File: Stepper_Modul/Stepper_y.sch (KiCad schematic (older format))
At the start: 14 parts, among them SW501 SW_DIP_x03, U501 TMC2226

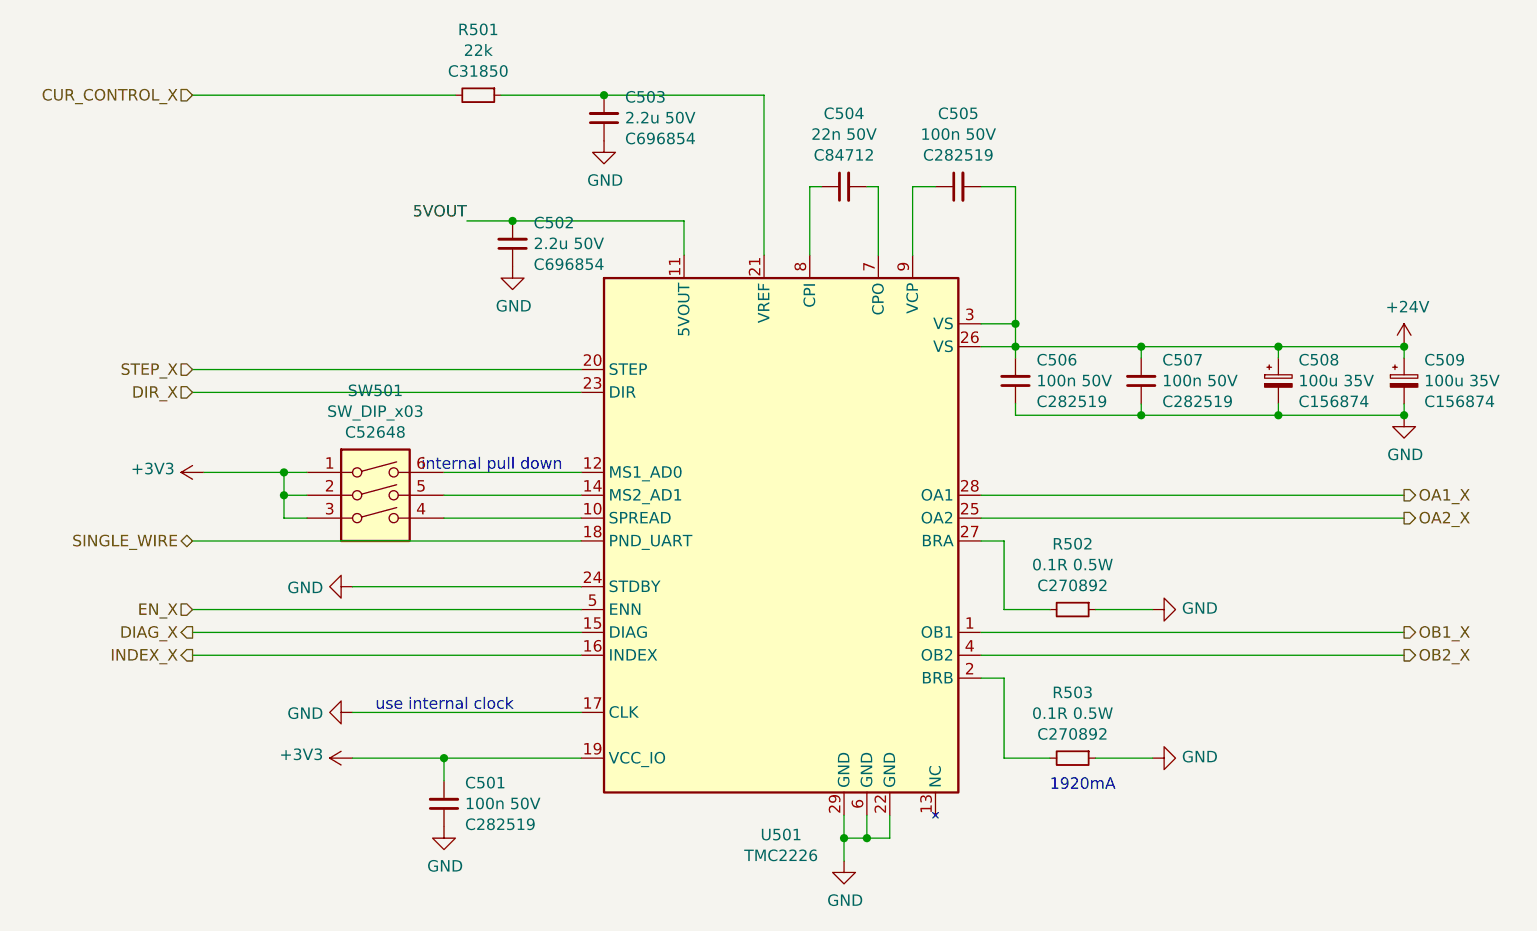
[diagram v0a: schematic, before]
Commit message: motor controller von stepper-treibern getrennt, sodass es modular ist. Libraries werden nun übergreifend von allen projekten verwendet
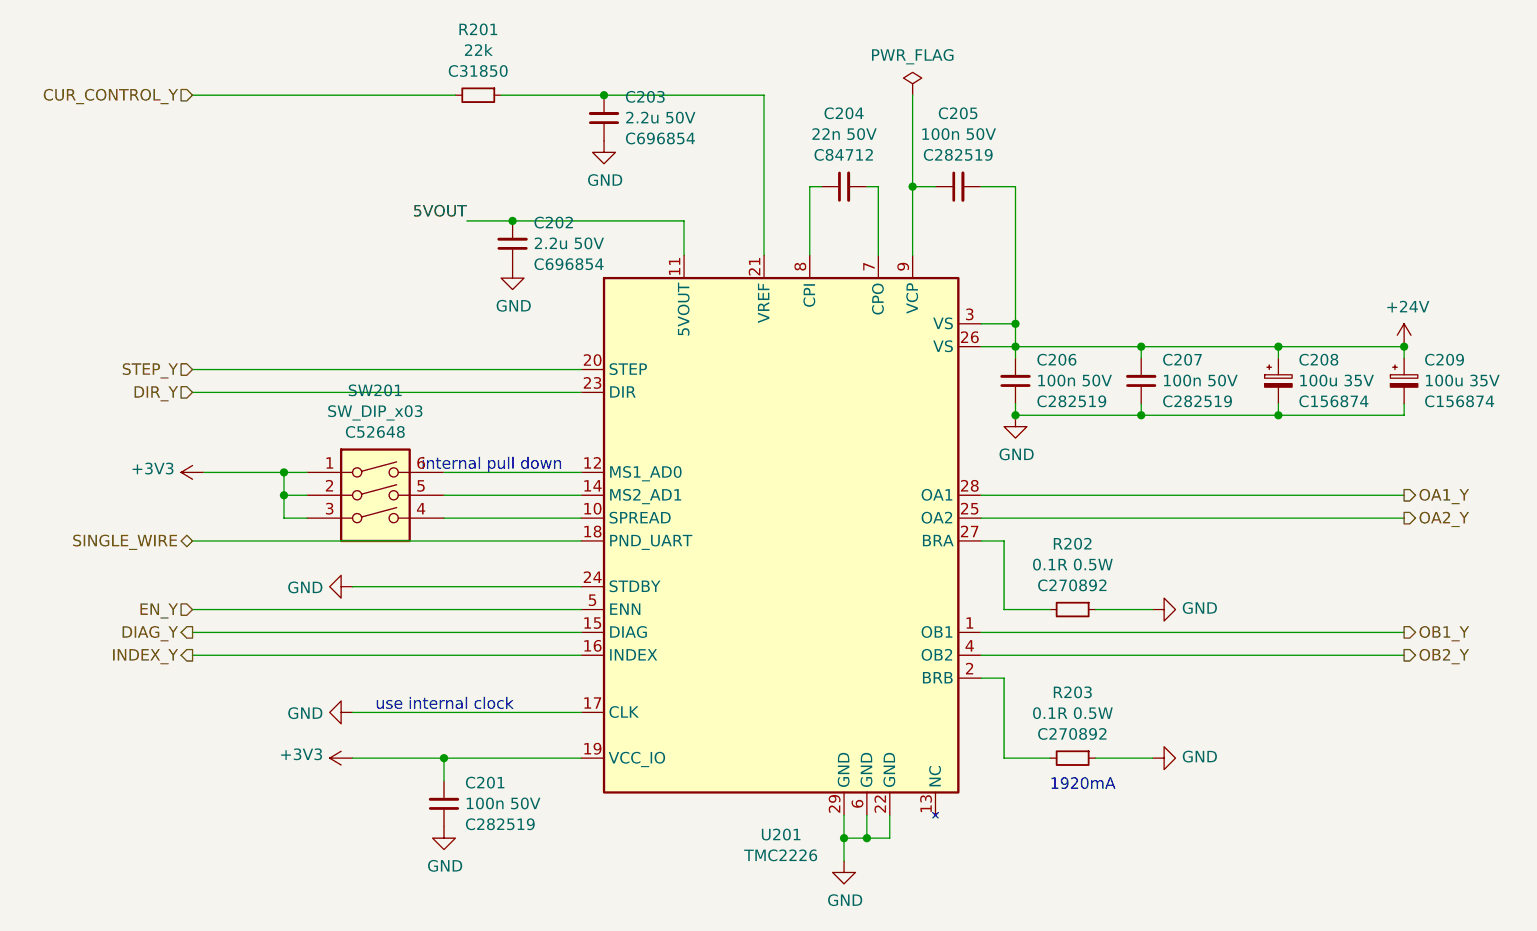
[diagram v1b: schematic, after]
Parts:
- removed C501, C505, C506, C507: 100n 50V, Capacitor_SMD:C_0603_1608Metric, symbol Device:C_Small
- removed C502, C503: 2.2u 50V, Capacitor_SMD:C_1210_3225Metric, symbol Device:C_Small
- removed C504: 22n 50V, Capacitor_SMD:C_0603_1608Metric, symbol Device:C_Small
- removed C508, C509: 100u 35V, Capacitor_THT:CP_Radial_D6.3mm_P2.50mm, symbol Device:CP_Small
- removed R501: 22k, Resistor_SMD:R_0603_1608Metric, symbol Device:R_Small
- removed R502, R503: 0.1R 0.5W, Resistor_SMD:R_1210_3225Metric, symbol Device:R_Small
- removed SW501: SW_DIP_x03, Package_DIP:DIP-6_W7.62mm, symbol Switch:SW_DIP_x03
- removed U501: TMC2226, Package_SO:TSSOP-28-1EP_4.4x9.7mm_P0.65mm, symbol StepperBoard-rescue:TMC2226-Pick_n_Place
- added C201, C205, C206, C207: 100n 50V, Capacitor_SMD:C_0603_1608Metric, symbol Device:C_Small
- added C202, C203: 2.2u 50V, Capacitor_SMD:C_1210_3225Metric, symbol Device:C_Small
- added C204: 22n 50V, Capacitor_SMD:C_0603_1608Metric, symbol Device:C_Small
- added C208, C209: 100u 35V, Capacitor_THT:CP_Radial_D6.3mm_P2.50mm, symbol Device:CP_Small
- added R201: 22k, Resistor_SMD:R_0603_1608Metric, symbol Device:R_Small
- added R202, R203: 0.1R 0.5W, Resistor_SMD:R_1210_3225Metric, symbol Device:R_Small
- added SW201: SW_DIP_x03, Package_DIP:DIP-6_W7.62mm, symbol Switch:SW_DIP_x03
- added U301: TMC2226, Package_SO:TSSOP-28-1EP_4.4x9.7mm_P0.65mm, symbol PorjectLibrary:TMC2226
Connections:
- net +24V: now also C205.2, C206.2, C207.2, C208.1, C209.1, U301.26 (VS), U301.3 (VS)
- net +3V3: now also C201.2, SW201.1, SW201.2, SW201.3, U301.19 (VCC_IO)
- net 5VOUT: now also C202.2, U301.11 (5VOUT)
- net GND: now also C201.1, C202.1, C203.1, C206.1, C207.1, C208.2, C209.2, R202.1, R203.1, U301.17 (CLK), U301.22 (GND), U301.24 (STDBY), U301.29 (GND), U301.6 (GND)
- net SINGLE_WIRE: now also U301.18 (PND_UART)
- new net: R203.2, U301.2 (BRB)
- new net: SW201.4, U301.10 (SPREAD)
- new net: SW201.6, U301.12 (MS1_AD0)
- new net: SW201.5, U301.14 (MS2_AD1)
- new net: C203.2, R201.1, U301.21 (VREF)
- new net: R202.2, U301.27 (BRA)
- new net: C204.2, U301.7 (CPO)
- new net: C204.1, U301.8 (CPI)
- new net: C205.1, U301.9 (VCP)
- new net CUR_CONTROL_Y: R201.2
- new net DIAG_Y: U301.15 (DIAG)
- new net DIR_Y: U301.23 (DIR)
- new net EN_Y: U301.5 (ENN)
- new net INDEX_Y: U301.16 (INDEX)
- new net OA1_Y: U301.28 (OA1)
- new net OA2_Y: U301.25 (OA2)
- new net OB1_Y: U301.1 (OB1)
- new net OB2_Y: U301.4 (OB2)
- new net STEP_Y: U301.20 (STEP)

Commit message: stepper board fertig gestellt
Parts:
- R201: value 22k -> 22K1; LCSC C31850 -> C137768
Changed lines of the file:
@@
 AR Path="/5FCAEEEC/5FCB624C" Ref="R?"  Part="1"
 F 0 "R201" V 5114 950 50  0000 C CNN
-F 1 "22k" V 5205 950 50  0000 C CNN
+F 1 "22K1" V 5205 950 50  0000 C CNN
 F 2 "Resistor_SMD:R_0603_1608Metric" H 5400 950 50  0001 C CNN
 F 3 "~" H 5400 950 50  0001 C CNN
-F 4 "C31850" V 5296 950 50  0000 C CNN "LCSC"
+F 4 "C137768" V 5296 950 50  0000 C CNN "LCSC"
 	1    5400 950
 	0    1    1    0

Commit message: BOM für LCSC überarbeitet. Tool für BOM export modifiziert
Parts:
- C208, C209: LCSC C156874 -> C45075
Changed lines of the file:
@@
 F 2 "Capacitor_THT:CP_Radial_D6.3mm_P2.50mm" H 8900 2200 50  0001 C CNN
 F 3 "https://datasheet.lcsc.com/szlcsc/Guangdong-TOPAZ-Elec-Tech-ECSS0608101M035P00_C156874.pdf" H 8900 2200 50  0001 C CNN
-F 4 "C156874" H 8988 2109 50  0000 L CNN "LCSC"
+F 4 "C45075" H 8988 2109 50  0000 L CNN "LCSC"
 	1    8900 2200
 	1    0    0    -1
@@
 F 2 "Capacitor_THT:CP_Radial_D6.3mm_P2.50mm" H 9450 2200 50  0001 C CNN
 F 3 "https://datasheet.lcsc.com/szlcsc/Guangdong-TOPAZ-Elec-Tech-ECSS0608101M035P00_C156874.pdf" H 9450 2200 50  0001 C CNN
-F 4 "C156874" H 9538 2109 50  0000 L CNN "LCSC"
+F 4 "C45075" H 9538 2109 50  0000 L CNN "LCSC"
 	1    9450 2200
 	1    0    0    -1

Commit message: Änderungen für bestellung V01 -  Bestellung abgeschickt
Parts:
- R202, R203: value 0.1R 0.5W -> 0.22R 0.5W; LCSC C270892 -> C159293
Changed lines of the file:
@@
 AR Path="/5FCAEEEC/5FCB6237" Ref="R?"  Part="1"
 F 0 "R202" V 7714 3200 50  0000 C CNN
-F 1 "0.1R 0.5W" V 7805 3200 50  0000 C CNN
+F 1 "0.22R 0.5W" V 7805 3200 50  0000 C CNN
 F 2 "Resistor_SMD:R_1210_3225Metric" H 8000 3200 50  0001 C CNN
 F 3 "~" H 8000 3200 50  0001 C CNN
-F 4 "C270892" V 7896 3200 50  0000 C CNN "LCSC"
+F 4 "C159293" V 7896 3200 50  0000 C CNN "LCSC"
 	1    8000 3200
 	0    1    1    0
@@
 AR Path="/5FCAEEEC/5FBD9462" Ref="R?"  Part="1"
 F 0 "R203" V 7714 3850 50  0000 C CNN
-F 1 "0.1R 0.5W" V 7805 3850 50  0000 C CNN
+F 1 "0.22R 0.5W" V 7805 3850 50  0000 C CNN
 F 2 "Resistor_SMD:R_1210_3225Metric" H 8000 3850 50  0001 C CNN
 F 3 "~" H 8000 3850 50  0001 C CNN
-F 4 "C270892" V 7896 3850 50  0000 C CNN "LCSC"
+F 4 "C159293" V 7896 3850 50  0000 C CNN "LCSC"
 	1    8000 3850
 	0    1    1    0
